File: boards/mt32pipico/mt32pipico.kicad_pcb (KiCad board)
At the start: 2 copper layers, 65 x 56 mm, 25 parts, among them J1 PWRIN, J10 VBUS, J2 ToPi, J3 ToMiSTer, J4 Relay, J5 MiSTerLED, J6 MiSTerSwitch, J7 ADC, J8 IO, J9 SWD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

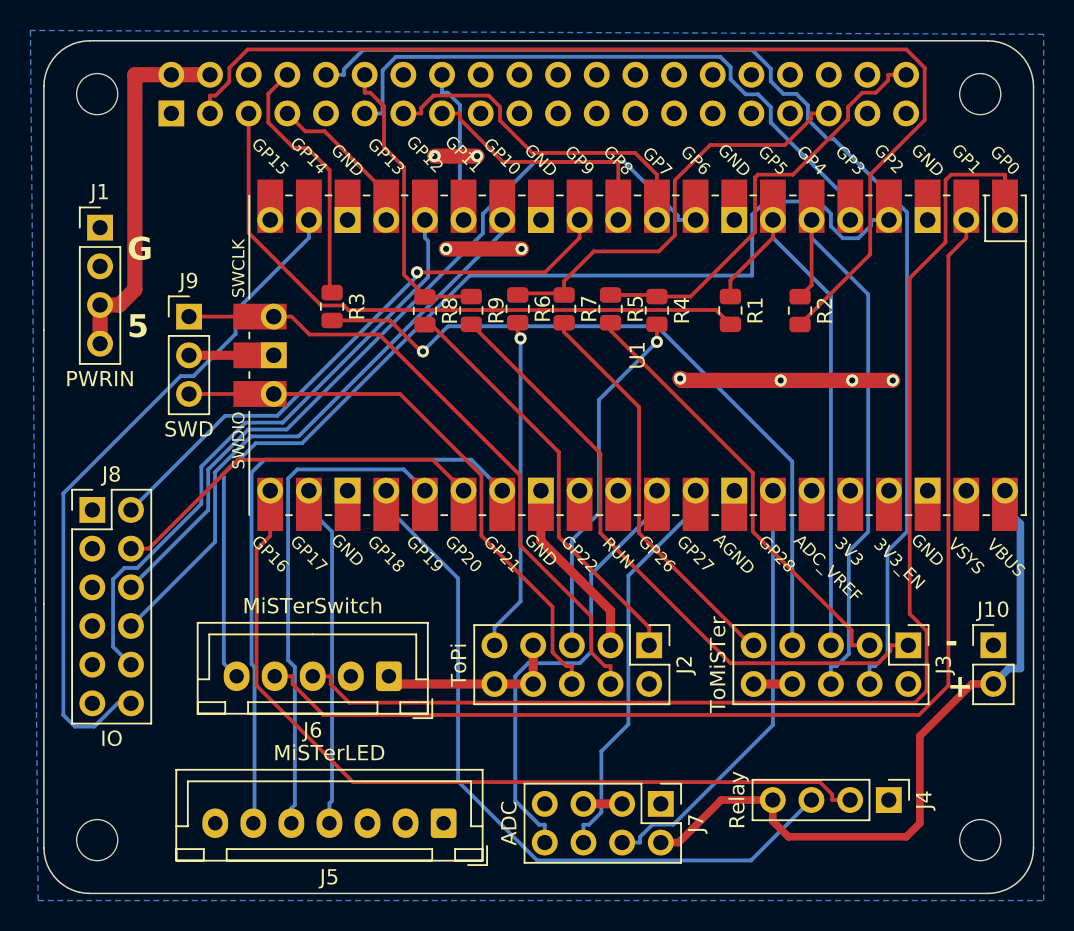
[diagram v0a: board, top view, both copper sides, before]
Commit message: Move to 14 pin headers for switch with off-board adapters
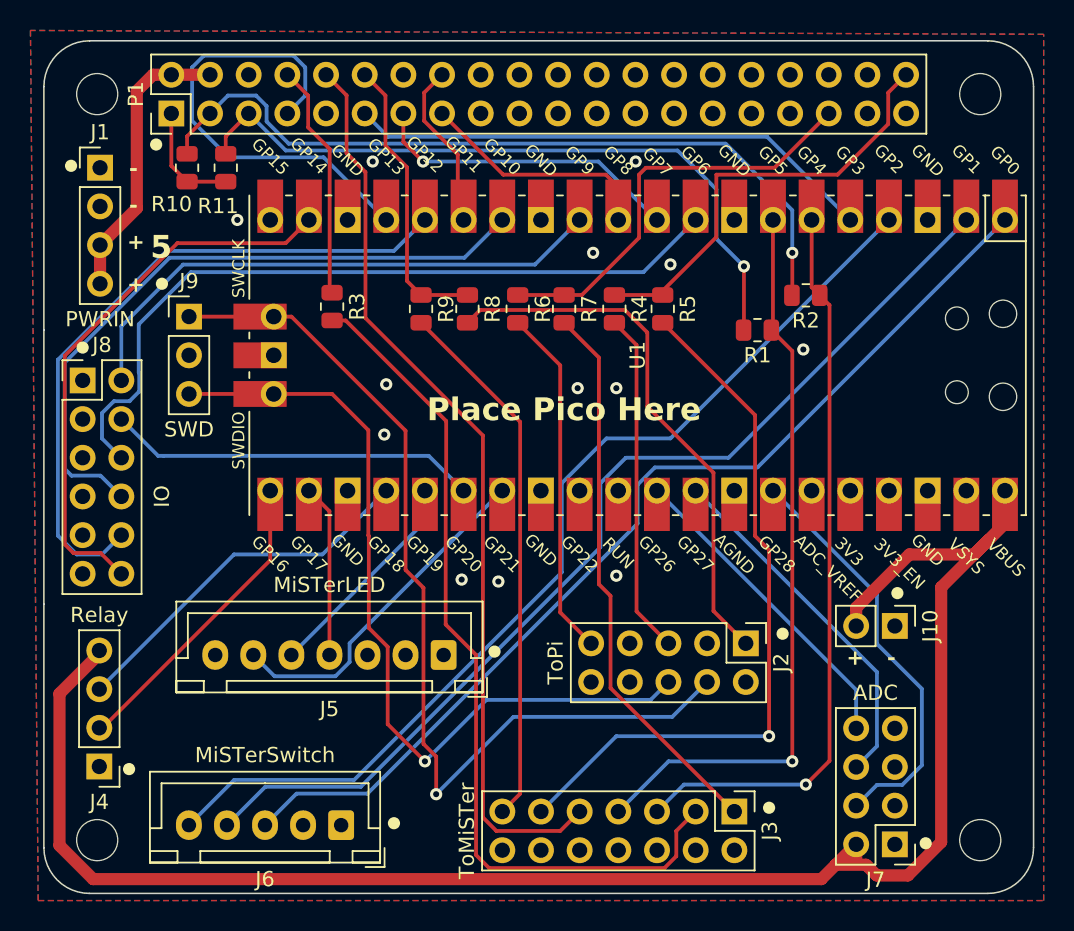
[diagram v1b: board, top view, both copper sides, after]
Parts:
- added R10: OPT, Resistor_SMD:R_0805_2012Metric, F.Cu at (194.2, 66.4)
- added R11: OPT, Resistor_SMD:R_0805_2012Metric, F.Cu at (196.7, 66.4)
- J3: footprint Connector_PinHeader_2.54mm:PinHeader_2x05_P2.54mm_Vertical -> Connector_PinHeader_2.54mm:PinHeader_2x07_P2.54mm_Vertical
- P1: footprint Connector_PinSocket_2.54mm:PinSocket_2x20_P2.54mm_Vertical -> Connector_PinHeader_2.54mm:PinHeader_2x20_P2.54mm_Vertical; moved to F.Cu
- U1: footprint MCU_RaspberryPi_and_Boards:RPi_Pico_SMD_TH_LOCAL -> MCU_RaspberryPi_and_Boards:RPi_Pico_SMD_TH
- moved J4 51.9 mm to (188.4, 105.8), turned to 180 degrees
- moved J3 15.8 mm to (230.1, 108.7)
- moved J7 15.6 mm to (240.7, 110.9), turned to 180 degrees
- moved J5 11.0 mm to (211.0, 98.4)
- moved J6 10.3 mm to (204.3, 109.6)
- moved J8 8.53 mm to (187.3, 80.4)
- moved J10 6.59 mm to (240.7, 96.5), turned to -90 degrees
- moved J2 6.35 mm to (230.9, 97.7)
- moved J1 3.94 mm to (188.5, 66.4)
- moved R5 3.43 mm to (225.4, 75.7)
- moved R9 3.30 mm to (209.6, 75.7)
- moved R8 2.80 mm to (212.6, 75.7)
- moved R4 2.80 mm to (222.2, 75.7)
- moved R1 2.20 mm to (231.6, 77.1), turned to 180 degrees
- moved R2 1.07 mm to (234.8, 74.8), turned to 180 degrees
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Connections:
- J3 pad 2: unconnected-(J3-Pin_2-Pad2) -> GND
- J3 pad 3: Net-(J3-Pin_3) -> /TXD
- J3 pad 4: /RXD -> GND
- J3 pad 5: /SCL -> /SDA
- J3 pad 6: /SDA -> GND
- J3 pad 7: /TXD -> /SCL
- J3 pad 9: Net-(J3-Pin_9) -> /RXD
- P1 pad 1: unconnected-(P1-Pin_1-Pad1) -> Net-(P1-Pin_1)
- R5 pad 2: Net-(J3-Pin_3) -> Net-(J3-Pin_11)
- R7 pad 2: Net-(J3-Pin_9) -> Net-(J3-Pin_1)
- R9 pad 2: Net-(J3-Pin_1) -> Net-(J3-Pin_13)
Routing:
- net /VBUS: track 46.6 -> 113.9 mm
- net GND: track 57.0 -> 0.00 mm, vias 8 -> 13
- net Net-(J3-Pin_11): track 0.00 -> 47.1 mm, vias 0 -> 1
- net Net-(J3-Pin_13): track 0.00 -> 35.3 mm
- net /RELAY1: track 55.5 -> 20.4 mm
- net Net-(J3-Pin_3): track 28.9 -> 0.00 mm
- net Net-(J3-Pin_9): track 26.4 -> 0.00 mm
- net /RELAY2: track 48.1 -> 24.2 mm
- net /SWCLK: track 42.4 -> 62.9 mm, vias 0 -> 1
- net /BTN5: track 10.4 -> 30.5 mm
- net Net-(P1-Pin_3): track 70.7 -> 51.3 mm, vias 0 -> 1
- net /LED_DISK: track 32.7 -> 14.4 mm
- net /LED_PWR: track 40.8 -> 22.7 mm
- net /BTN_RESET: track 83.7 -> 66.6 mm
- net /RXD: track 76.7 -> 60.3 mm
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- added copper zone on F.Cu, net GND
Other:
- board text added: "Place Pico Here"
- board text removed: "G"
